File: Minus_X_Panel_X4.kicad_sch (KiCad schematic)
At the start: 0 parts

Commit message: Symbol, Footprint and 3D added for GPS connector
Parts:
- added J1: SM05B-SRSS-TB_LF__SN_, Custom-Footprints:JST_SM05B-SRSS-TB_LF__SN_, symbol Custom-Symbols:SM05B-SRSS-TB_LF__SN_
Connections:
- new net: J1.S1 (SHIELD), J1.S2 (SHIELD)
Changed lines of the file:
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@@
 	(generator_version "9.0")
 	(paper "A4")
+	(symbol
+		(lib_id "Custom-Symbols:SM05B-SRSS-TB_LF__SN_")
+		(at 86.36 90.17 0)
+		(unit 1)
+		(exclude_from_sim no)
+		(in_bom yes)
+		(on_board yes)
+		(dnp no)
+		(fields_autoplaced yes)
+		(property "Reference" "J1"
+			(at 92.71 88.8999 0)
+			(effects
+				(font
+					(size 1.27 1.27)
+				)
+				(justify left)
+			)
+		)
+		(property "Value" "SM05B-SRSS-TB_LF__SN_"
+			(at 92.71 91.4399 0)
+			(effects
+				(font
+					(size 1.27 1.27)
+				)
+				(justify left)
+			)
+		)
+		(property "Footprint" "Custom-Footprints:JST_SM05B-SRSS-TB_LF__SN_"
+			(at 86.36 90.17 0)
+			(effects
+				(font
+					(size 1.27 1.27)
+				)
+				(justify bottom)
+				(hide yes)
+			)
+		)
+		(property "Datasheet" ""
+			(at 86.36 90.17 0)
+			(effects
+				(font
+					(size 1.27 1.27)
+				)
+				(hide yes)
+			)
+		)
+		(property "Description" ""
+			(at 86.36 90.17 0)
+			(effects
+				(font
+					(size 1.27 1.27)
+				)
+				(hide yes)
+			)
+		)
+		(property "MF" ""
+			(at 86.36 90.17 0)
+			(effects
+				(font
+					(size 1.27 1.27)
+				)
+				(justify bottom)
+				(hide yes)
+			)
+		)
+		(property "Description_1" ""
+			(at 86.36 90.17 0)
+			(effects
+				(font
+					(size 1.27 1.27)
+				)
+				(justify bottom)
+				(hide yes)
+			)
+		)
+		(property "Package" ""
+			(at 86.36 90.17 0)
+			(effects
+				(font
+					(size 1.27 1.27)
+				)
+				(justify bottom)
+				(hide yes)
+			)
+		)
+		(property "Price" ""
+			(at 86.36 90.17 0)
+			(effects
+				(font
+					(size 1.27 1.27)
+				)
+				(justify bottom)
+				(hide yes)
+			)
+		)
+		(property "Check_prices" ""
+			(at 86.36 90.17 0)
+			(effects
+				(font
+					(size 1.27 1.27)
+				)
+				(justify bottom)
+				(hide yes)
+			)
+		)
+		(property "STANDARD" ""
+			(at 86.36 90.17 0)
+			(effects
+				(font
+					(size 1.27 1.27)
+				)
+				(justify bottom)
+				(hide yes)
+			)
+		)
+		(property "SnapEDA_Link" ""
+			(at 86.36 90.17 0)
+			(effects
+				(font
+					(size 1.27 1.27)
+				)
+				(justify bottom)
+				(hide yes)
+			)
+		)
+		(property "MP" ""
+			(at 86.36 90.17 0)
+			(effects
+				(font
+					(size 1.27 1.27)
+				)
+				(justify bottom)
+				(hide yes)
+			)
+		)
+		(property "Availability" ""
+			(at 86.36 90.17 0)
+			(effects
+				(font
+					(size 1.27 1.27)
+				)
+				(justify bottom)
+				(hide yes)
+			)
+		)
+		(property "MANUFACTURER" ""
+			(at 86.36 90.17 0)
+			(effects
+				(font
+					(size 1.27 1.27)
+				)
+				(justify bottom)
+				(hide yes)
+			)
+		)
+		(pin "4"
+		)
+		(pin "2"
+		)
+		(pin "1"
+		)
+		(pin "S1"
+		)
+		(pin "5"
+		)
+		(pin "3"
+		)
+		(pin "S2"
+		)
+		(instances
+			(project ""
+				(path "/77059503-81f8-4d9e-9911-eb47cebf537f"
+					(reference "J1")
+					(unit 1)
+				)
+			)
+		)
+	)
 	(sheet_instances
 		(path "/"

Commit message: Symbol and foot print id almost ready
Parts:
- removed J1: SM05B-SRSS-TB_LF__SN_, Custom-Footprints:JST_SM05B-SRSS-TB_LF__SN_, symbol Custom-Symbols:SM05B-SRSS-TB_LF__SN_
- added D1, D2, D3, D4: CUHS20S30,H3F, Custom-Footprints:CUHS20S30,H3F, symbol Custom-Symbols:CUHS20S30,H3F
- added S1, S4: solar_cell_B, Custom-Footprints:solar_cell_B, symbol Custom-Symbols:solar_cell_B
- added S2, S3: Solar_cell_C, Custom-Footprints:solar_cell_C, symbol Custom-Symbols:Solar_cell_C
- added U$1: 2PIN_FEMALE, Custom-Footprints:FSR-41057-02-F, symbol Custom-Symbols:2PIN_FEMALE
- added U$2: 3PIN_FEMALE_-XC3PIN_MALE, Custom-Footprints:FSR-41057-03-F, symbol Custom-Symbols:3PIN_FEMALE_-XC3PIN_MALE
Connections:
- new net: D4.2 (A), S1.+V
- new net: S1.GND, S4.+V
- new net: D4.1 (K), U$2.PWR, U$2.SUNS
- new net: D3.1 (K), U$2.PWR1
- new net: D2.1 (K), D3.2 (A), S3.+V
- new net: D1.1 (K), S2.+V, S4.GND
- new net GND: D1.2 (A), D2.2 (A), S2.GND, S3.GND, U$1.GND, U$1.GND1

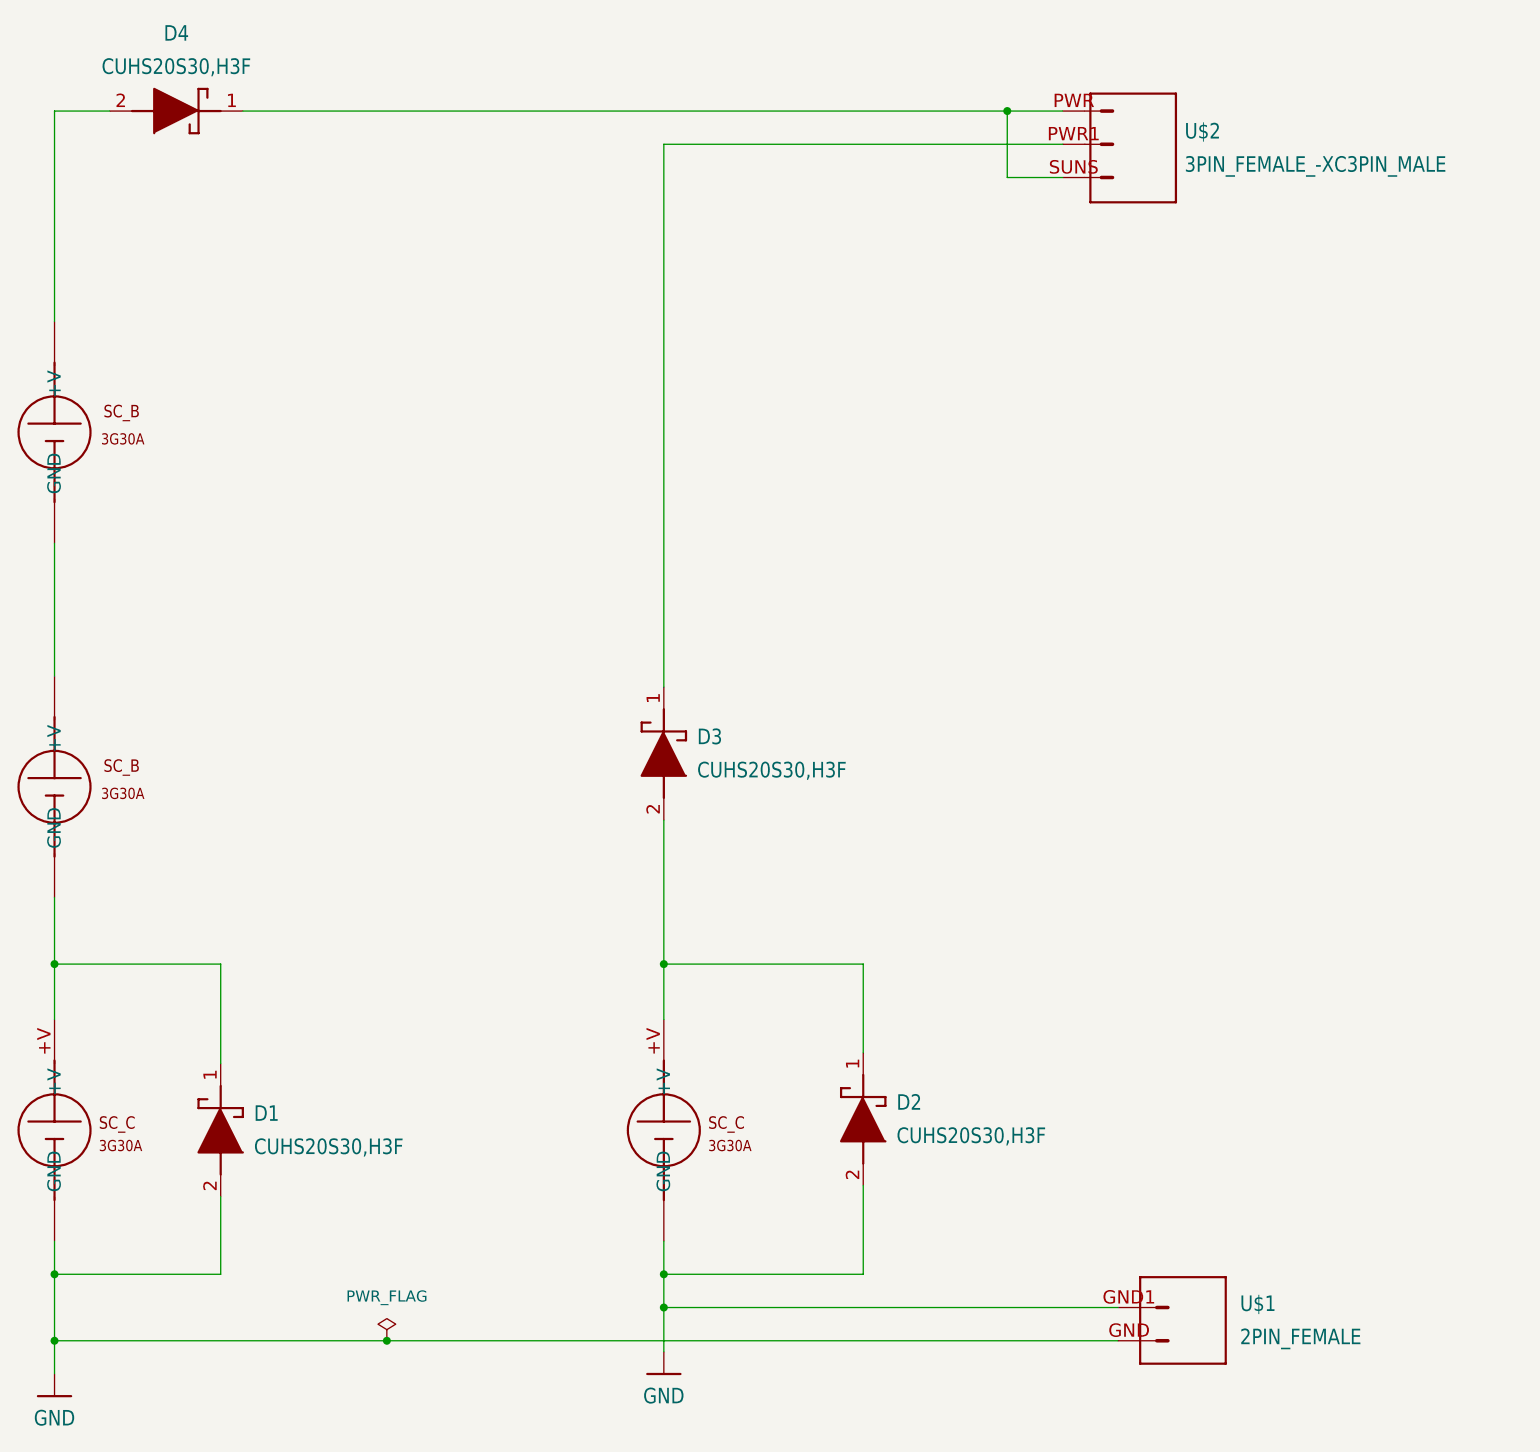
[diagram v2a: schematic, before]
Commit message: i updateed the PCB configuration of the panel
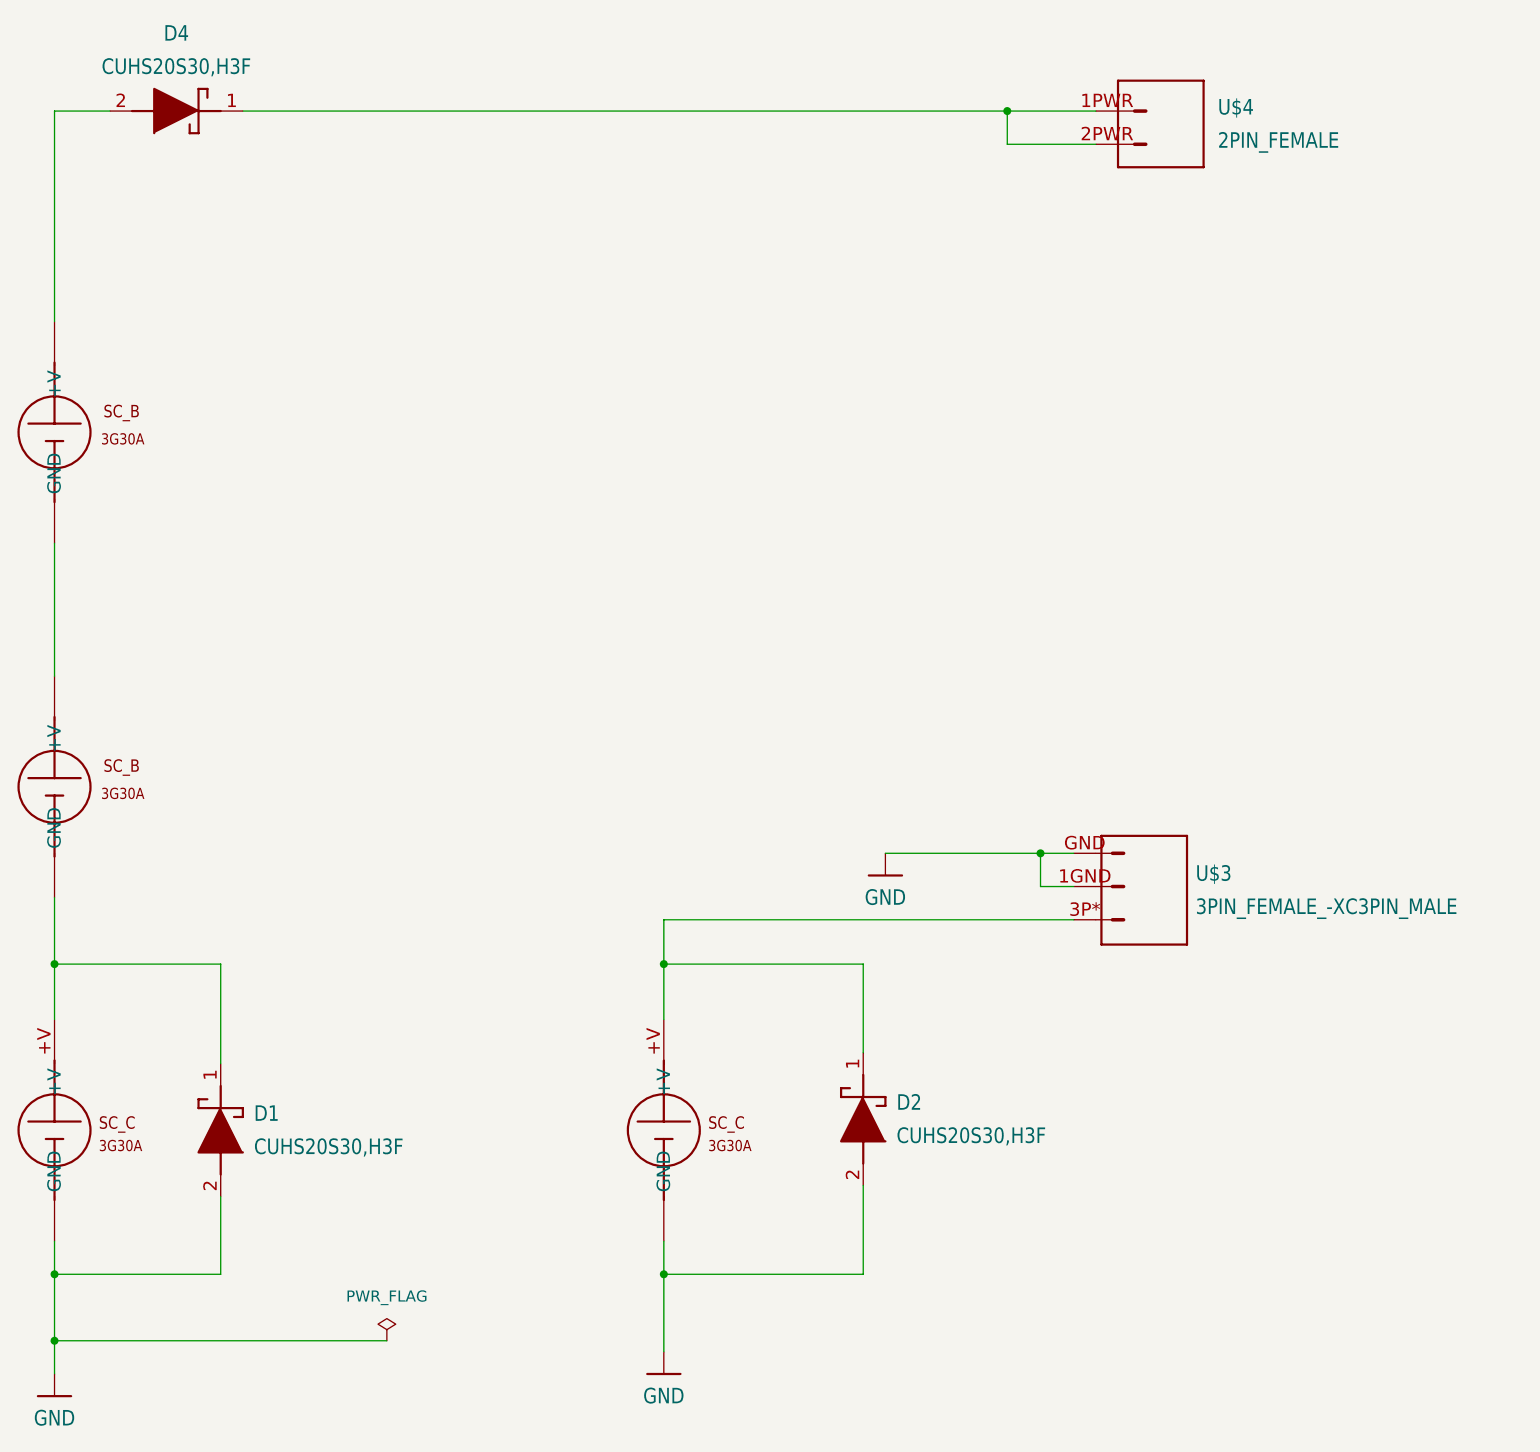
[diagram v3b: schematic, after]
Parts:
- removed D3: CUHS20S30,H3F, Custom-Footprints:CUHS20S30,H3F, symbol Custom-Symbols:CUHS20S30,H3F
- removed U$1: 2PIN_FEMALE, Custom-Footprints:FSR-41057-02-F, symbol Custom-Symbols:2PIN_FEMALE
- removed U$2: 3PIN_FEMALE_-XC3PIN_MALE, Custom-Footprints:FSR-41057-03-F, symbol Custom-Symbols:3PIN_FEMALE_-XC3PIN_MALE
- added U$3: 3PIN_FEMALE_-XC3PIN_MALE, Custom-Footprints:FSR-41057-03-F, symbol Custom-Symbols:3PIN_FEMALE_-XC3PIN_MALE
- added U$4: 2PIN_FEMALE, Custom-Footprints:FSR-41057-02-F, symbol Custom-Symbols:2PIN_FEMALE
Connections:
- net GND: now also U$3.1GND, U$3.GND
- net at D4.1 (K): now also U$4.1PWR, U$4.2PWR
- net at D2.1 (K), S3.+V: now also U$3.3P*

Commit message: -X Panel last updated the tracks
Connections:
- net +VC: now reaches D4.2 (A), S1.+V
- net +VB: now reaches S1.GND, S4.+V
- net +VD: now reaches D2.1 (K), S3.+V, U$3.3P*
- net +VA: now reaches D1.1 (K), S2.+V, S4.GND
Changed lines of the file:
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@@
+		)
+	)
+	(label "+VC"
+		(at 38.1 53.34 0)
+		(effects
+			(font
+				(size 1.27 1.27)
+			)
+			(justify left bottom)
+		)
+	)
+	(label "+VB"
+		(at 38.1 102.87 0)
+		(effects
+			(font
+				(size 1.27 1.27)
+			)
+			(justify left bottom)
+		)
+	)
+	(label "+VA"
+		(at 38.1 143.51 0)
+		(effects
+			(font
+				(size 1.27 1.27)
+			)
+			(justify left bottom)
+		)
+	)
+	(label "+VD"
+		(at 107.95 137.16 0)
+		(effects
+			(font
+				(size 1.27 1.27)
+			)
+			(justify left bottom)
 		)
 	)
